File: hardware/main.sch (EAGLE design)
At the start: 18 parts

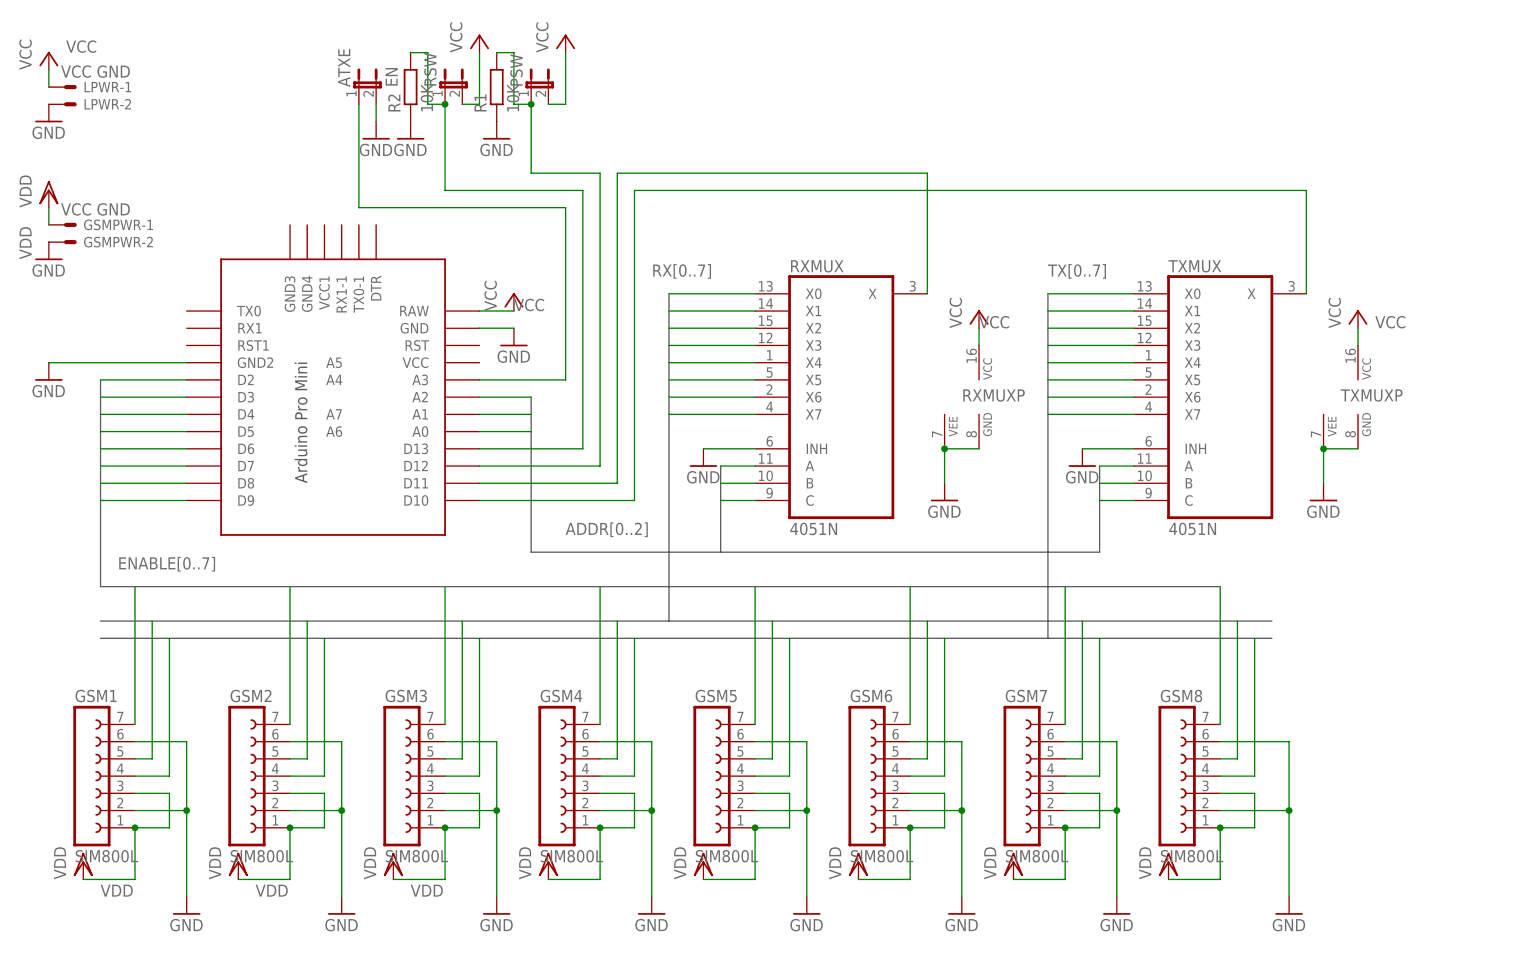
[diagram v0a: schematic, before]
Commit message: adding extra power supply for GSM, and connecting to gsm power through a jumper
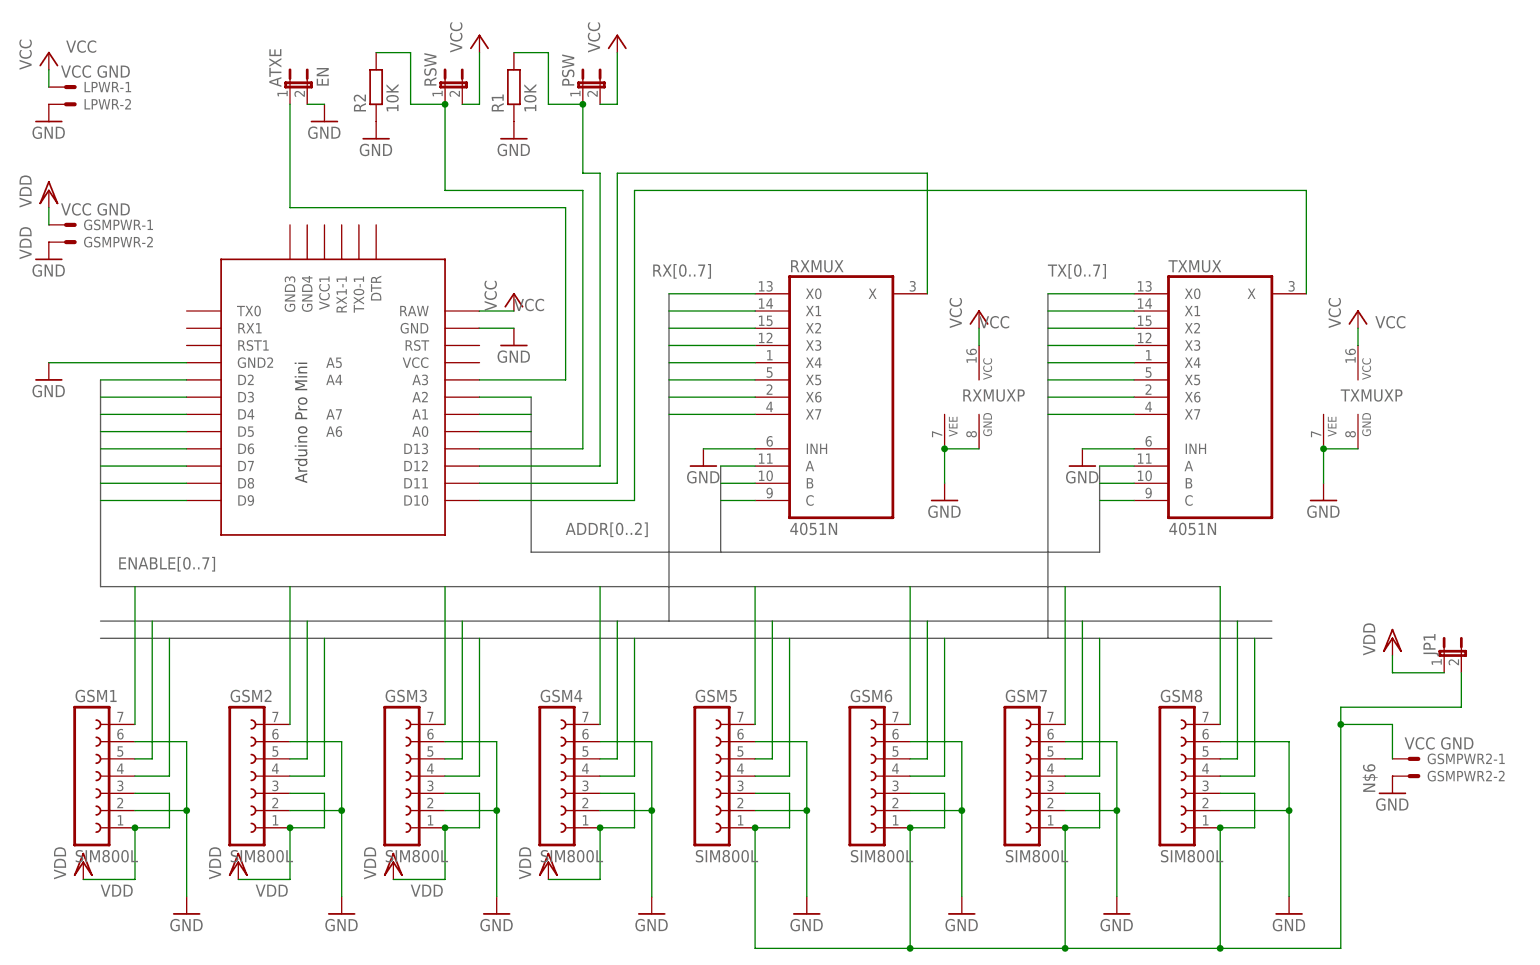
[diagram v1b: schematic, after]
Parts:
- added GSMPWR2: VCC GND, con-molex:22-23-2021
- added JP1: (no value), jumper:JP1E
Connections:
- new net N$6: GSM5.1, GSM5.3, GSM6.1, GSM6.3, GSM7.1, GSM7.3, GSM8.1, GSM8.3, GSMPWR2-1.S, JP1.2
- net GND: now also GSMPWR2-2.S
- net VDD: now also JP1.1; no longer GSM5.1, GSM5.3, GSM6.1, GSM6.3, GSM7.1, GSM7.3, GSM8.1, GSM8.3
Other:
- moved on the sheet: ATXE, PSW, R1, R2
